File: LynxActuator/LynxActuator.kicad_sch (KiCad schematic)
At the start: 20 parts, among them M1 Motor_DC, U1 ELR1-SC-24DC, U2 E-STOP

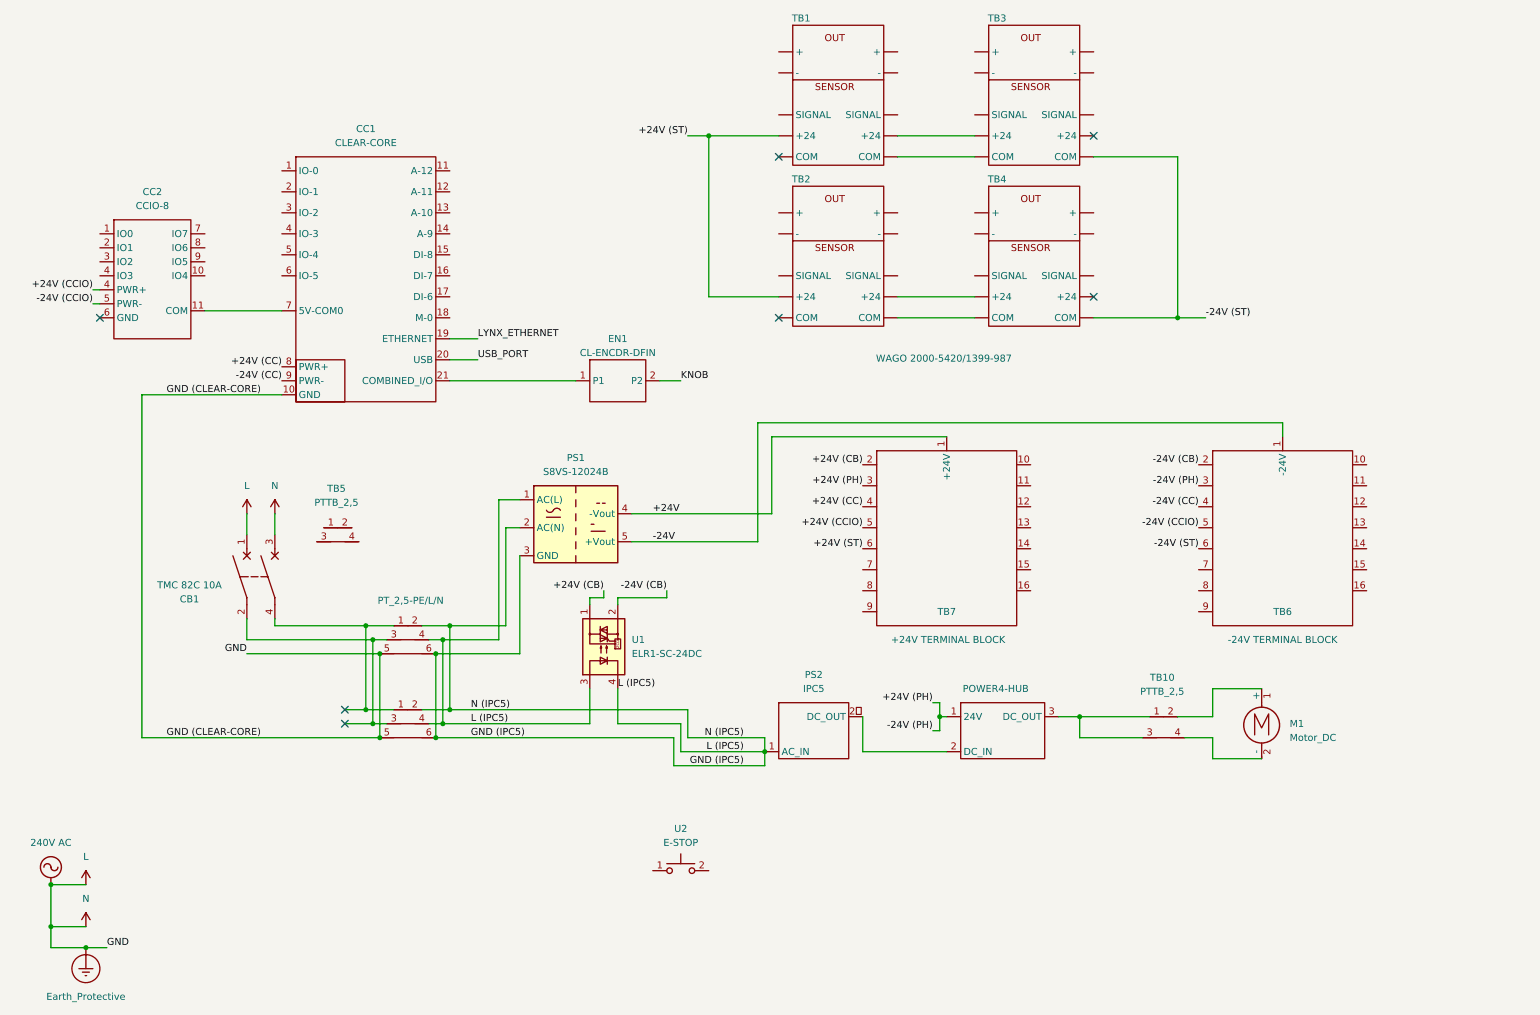
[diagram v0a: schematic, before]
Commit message: Update PCB + Add Lynx Wiring Diagram
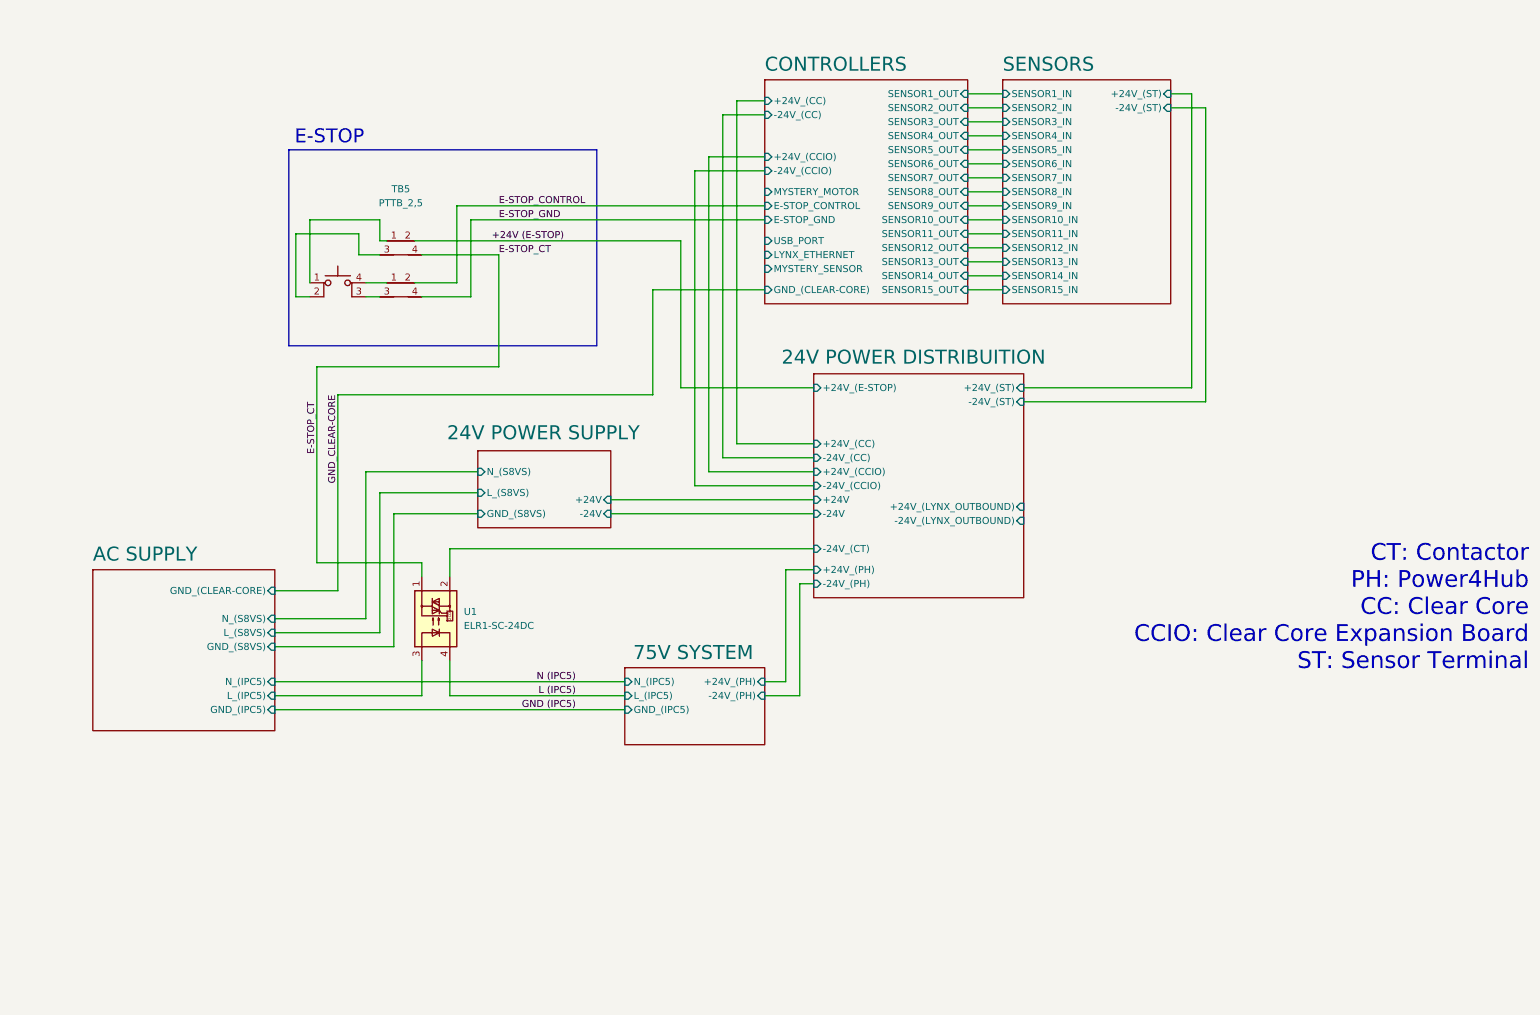
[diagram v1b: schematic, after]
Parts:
- removed CB1: TMC 82C 10A, symbol LynxActuatorSymbols:TMC-82C-10A
- removed CC1: CLEAR-CORE, symbol LynxActuatorSymbols:CLEAR-CORE
- removed CC2: CCIO-8, symbol LynxActuatorSymbols:CCIO-8
- removed EN1: CL-ENCDR-DFIN, symbol LynxActuatorSymbols:CL-ENCDR-DFIN
- removed M1: Motor_DC, symbol Motor:Motor_DC
- removed PH1: POWER4-HUB, symbol LynxActuatorSymbols:POWER4-HUB
- removed PS1: S8VS-12024B, symbol LynxActuatorSymbols:S8VS-12024B
- removed PS2: IPC5, symbol LynxActuatorSymbols:IPC5
- removed TB1, TB2, TB3, TB4: WAGO 2000-5420/1399-987, symbol LynxActuatorSymbols:WAGO-2000-5420
- removed TB10: PTTB_2,5, symbol LynxActuatorSymbols:PTTB_2,5
- removed TB6: -24V TERMINAL BLOCK, symbol LynxActuatorSymbols:24V-BLOCK-
- removed TB7: +24V TERMINAL BLOCK, symbol LynxActuatorSymbols:24V-BLOCK+
- removed TB8, TB9: PT_2,5-PE/L/N, symbol LynxActuatorSymbols:PT_2,5-PE/L/N
- removed U2: E-STOP, symbol LynxActuatorSymbols:E-STOP
- added SW1: E-STOP, symbol Switch:SW_MEC_5E
- added TB12: PTTB_2,5, symbol LynxActuatorSymbols:PTTB_2,5
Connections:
- net +24V (CB) is gone; now on net E-STOP_CT: U1.1
- net GND (IPC5): no longer U1.3, U1.4
- net at TB5.1: now also SW1.1
- net +24V (E-STOP): now reaches TB5.2
- net at TB5.3: now also SW1.2
- net E-STOP_CT: now reaches TB5.4
- net -24V (CB) renamed 24V POWER DISTRIBUITION/-24V_(CT)
- new net: SW1.3 (K), TB12.3
- new net: SW1.4 (A), TB12.1
- new net AC SUPPLY/L_(IPC5): U1.3
- new net E-STOP_CONTROL: TB12.2
- new net E-STOP_GND: TB12.4
- new net L (IPC5): U1.4
- no-connect marks 7 -> 0
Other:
- added sheet 24V POWER DISTRIBUITION (24v.kicad_sch)
- added sheet 24V POWER SUPPLY (25v_power_supply.kicad_sch)
- added sheet 75V SYSTEM (75v.kicad_sch)
- added sheet AC SUPPLY (ac_supply.kicad_sch)
- added sheet CONTROLLERS (controllers.kicad_sch)
- added sheet SENSORS (sensors.kicad_sch)
- note added: "CT: Contactor PH: Power4Hub CC: Clear Core CCIO: Clear Core Expansion Board ST: Sensor Terminal"
- note added: "E-STOP"
- moved on the sheet: TB5, U1

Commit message: Visual Edits
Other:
- sheet CONTROLLERS ports: added PRESSURE_SENSOR, RAIL_MOTOR; removed MYSTERY_MOTOR, MYSTERY_SENSOR

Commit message: Add updated layout
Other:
- sheet CONTROLLERS renamed CLEAR CORE
- sheet 24V POWER DISTRIBUITION ports: added none; removed +24V_(ST), -24V_(ST)
- sheet SENSORS ports: added none; removed +24V_(ST), -24V_(ST)
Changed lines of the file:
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@@
 	(wire
 		(pts
-			(xy 231.14 29.21) (xy 224.79 29.21)
-		)
-		(stroke
-			(width 0)
-			(type default)
-		)
-	)
-	(wire
-		(pts
 			(xy 187.96 22.86) (xy 194.31 22.86)
 		)
@@
 	(wire
 		(pts
-			(xy 228.6 80.01) (xy 228.6 26.67)
-		)
-		(stroke
-			(width 0)
-			(type default)
-		)
-	)
-	(wire
-		(pts
 			(xy 81.28 53.34) (xy 82.55 53.34)
 		)
@@
 	(wire
 		(pts
-			(xy 198.12 82.55) (xy 231.14 82.55)
-		)
-		(stroke
-			(width 0)
-			(type default)
-		)
-	)
-	(wire
-		(pts
 			(xy 160.02 97.79) (xy 138.43 97.79)
 		)
@@
 	(wire
 		(pts
-			(xy 187.96 67.31) (xy 241.3 67.31)
+			(xy 187.96 67.31) (xy 229.87 67.31)
 		)
 		(stroke
@@
 	(wire
 		(pts
-			(xy 198.12 80.01) (xy 228.6 80.01)
-		)
-		(stroke
-			(width 0)
-			(type default)
-		)
-	)
-	(wire
-		(pts
 			(xy 87.63 60.96) (xy 95.25 60.96)
 		)
@@
 	(wire
 		(pts
-			(xy 198.12 87.63) (xy 241.3 87.63)
+			(xy 198.12 87.63) (xy 229.87 87.63)
 		)
 		(stroke
@@
 	(wire
 		(pts
-			(xy 198.12 85.09) (xy 241.3 85.09)
+			(xy 198.12 85.09) (xy 229.87 85.09)
 		)
 		(stroke
@@
 	(wire
 		(pts
-			(xy 187.96 62.23) (xy 241.3 62.23)
+			(xy 187.96 62.23) (xy 229.87 62.23)
 		)
 		(stroke
@@
 	(wire
 		(pts
-			(xy 187.96 69.85) (xy 241.3 69.85)
-		)
-		(stroke
-			(width 0)
-			(type default)
-		)
-	)
-	(wire
-		(pts
-			(xy 231.14 82.55) (xy 231.14 29.21)
+			(xy 187.96 69.85) (xy 229.87 69.85)
 		)
 		(stroke
@@
 	(wire
 		(pts
-			(xy 187.96 64.77) (xy 241.3 64.77)
+			(xy 187.96 64.77) (xy 229.87 64.77)
 		)
 		(stroke
@@
 	(wire
 		(pts
-			(xy 228.6 26.67) (xy 224.79 26.67)
-		)
-		(stroke
-			(width 0)
-			(type default)
-		)
-	)
-	(wire
-		(pts
 			(xy 160.02 109.22) (xy 93.98 109.22)
 		)
@@
 	)
 	(label "+24V_(LYNX_OUTBOUND)"
-		(at 241.3 85.09 0)
+		(at 229.87 85.09 0)
 		(effects
 			(font
@@
 	)
 	(label "LYNX_ETHERNET"
-		(at 241.3 67.31 0)
+		(at 229.87 67.31 0)
 		(effects
 			(font
@@
 	)
 	(label "RAIL_MOTOR"
-		(at 241.3 62.23 0)
+		(at 229.87 62.23 0)
 		(effects
 			(font
@@
 	)
 	(label "-24V_(LYNX_OUTBOUND)"
-		(at 241.3 87.63 0)
+		(at 229.87 87.63 0)
 		(effects
 			(font
@@
 	)
 	(label "PRESSURE_SENSOR"
-		(at 241.3 69.85 0)
+		(at 229.87 69.85 0)
 		(effects
 			(font
@@
 	)
 	(label "USB_PORT"
-		(at 241.3 64.77 0)
+		(at 229.87 64.77 0)
 		(effects
 			(font
@@
 			)
 		)
-		(pin "-24V_(ST)" input
-			(at 224.79 29.21 0)
-			(effects
-				(font
-					(size 1.27 1.27)
-				)
-				(justify right)
-			)
-		)
-		(pin "+24V_(ST)" input
-			(at 224.79 26.67 0)
-			(effects
-				(font
-					(size 1.27 1.27)
-				)
-				(justify right)
-			)
-		)
 		(pin "SENSOR10_IN" input
 			(at 194.31 45.72 180)
@@
 			(color 0 0 0 0.0000)
 		)
-		(property "Sheetname" "CONTROLLERS"
+		(property "Sheetname" "CLEAR CORE"
 			(at 151.13 18.288 0)
 			(effects
@@
 			)
 		)
-		(pin "+24V_(ST)" input
-			(at 198.12 80.01 0)
-			(effects
-				(font
-					(size 1.27 1.27)
-				)
-				(justify right)
-			)
-		)
 		(pin "-24V_(LYNX_OUTBOUND)" input
 			(at 198.12 87.63 0)
@@
 			)
 		)
-		(pin "-24V_(ST)" input
-			(at 198.12 82.55 0)
-			(effects
-				(font
-					(size 1.27 1.27)
-				)
-				(justify right)
-			)
-		)
